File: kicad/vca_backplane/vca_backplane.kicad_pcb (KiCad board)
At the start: 4 copper layers, 147.2 x 109.9 mm, 98 parts, among them J1 Conn_02x20_Odd_Even, J10 AudioJack3DPDT, J2 Eurorack Power, J3 Conn_02x20_Odd_Even, J4 Conn_02x20_Odd_Even, J5 Conn_02x20_Odd_Even, J6 Conn_02x20_Odd_Even, J7 Conn_02x20_Odd_Even, J8 Conn_02x20_Odd_Even, J9 AudioJack3DPDT, Q1 DMMT5401, Q2 DMG2305UX, Q3 BSS138, Q4 BSS138, U1 74HCT138, U10 NE5532, U11 74HCT138, U12 MAX333A, U13 MAX333A, U14 NE5532, U2 74HCT245, U3 74LVC245, U4 MCP4822, U5 PCA9555PW, U7 AS3360, U8 M24C02-WMN, U9 PS508

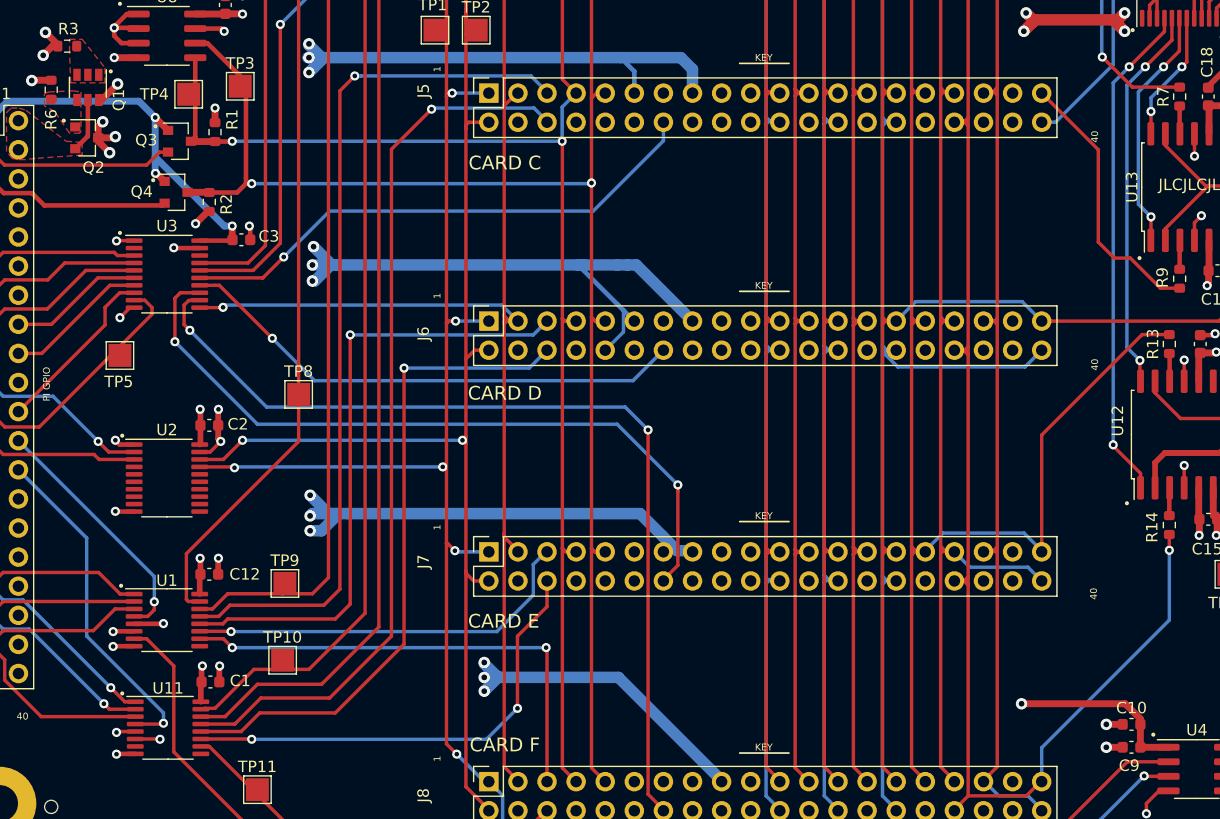
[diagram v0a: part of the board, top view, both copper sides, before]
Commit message: fix library dependency
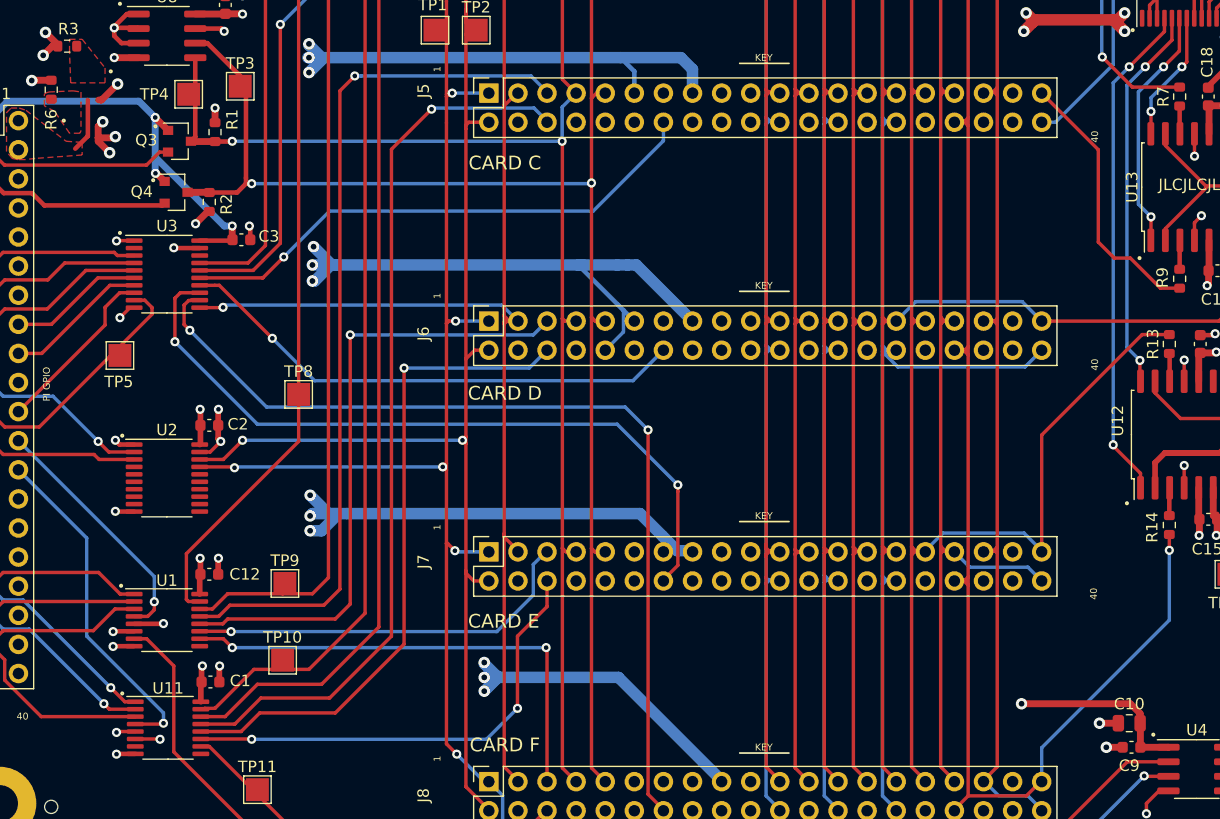
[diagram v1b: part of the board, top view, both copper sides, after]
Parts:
- removed Q1: DMMT5401, Package_TO_SOT_SMD:SOT-23-6
- removed Q2: DMG2305UX, Package_TO_SOT_SMD:SOT-23
- C10: footprint Capacitor_SMD:C_0603_1608Metric -> Capacitor_SMD:C_0805_2012Metric
- moved C10 0.22 mm to (132.9, 131.9)

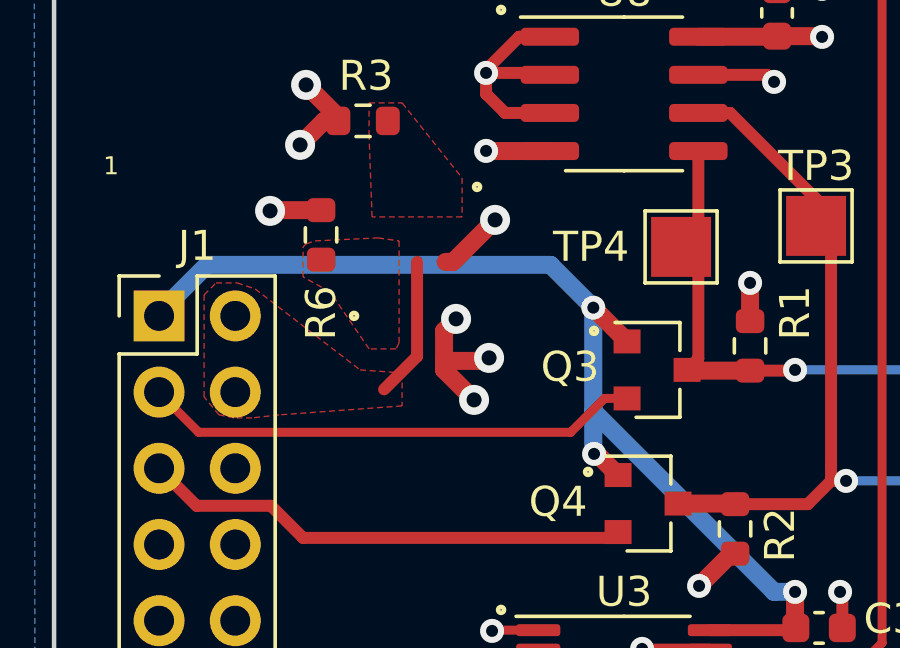
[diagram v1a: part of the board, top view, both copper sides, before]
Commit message: add missing components after library fix
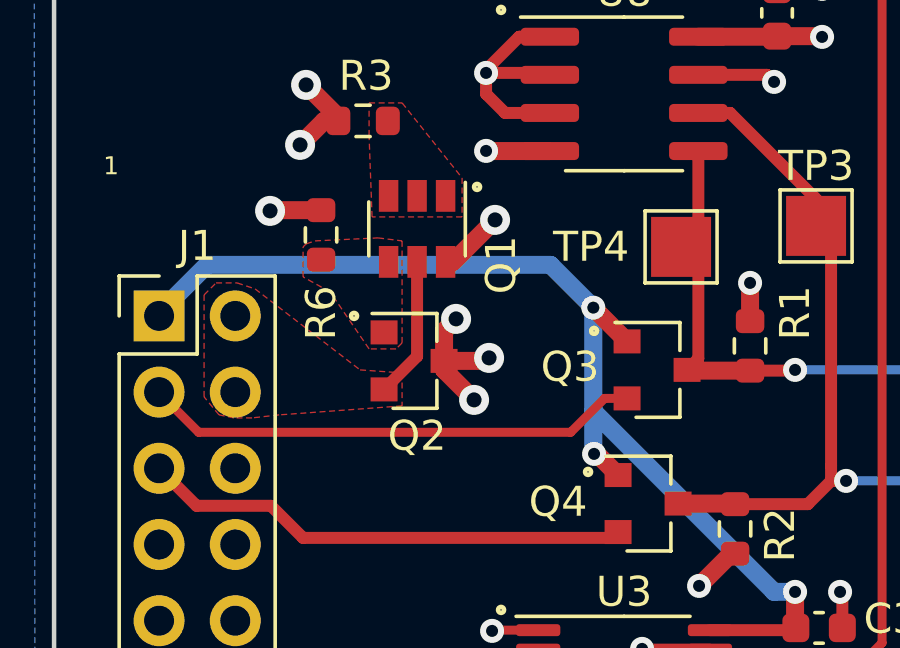
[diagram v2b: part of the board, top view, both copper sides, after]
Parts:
- added Q1: DMMT5401, Package_TO_SOT_SMD:SOT-23-6, F.Cu at (42.0, 76.4)
- added Q2: DMG2305UX, Package_TO_SOT_SMD:SOT-23, F.Cu at (41.9, 80.8)
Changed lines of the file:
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@@
     (tracks 2272)
     (zones 0)
-    (modules 96)
+    (modules 98)
     (nets 163)
   )
@@
   )
   (setup
-    (last_trace_width 0.6)
+    (last_trace_width 0.4)
     (user_trace_width 0.2)
     (user_trace_width 0.3)
@@
   (net 159 "Net-(R11-Pad2)")
   (net 160 "Net-(D1-Pad1)")
-  (net 161 "Net-(R3-Pad1)")
-  (net 162 "Net-(R6-Pad1)")
+  (net 161 "Net-(Q1-Pad4)")
+  (net 162 "Net-(Q1-Pad1)")
   (net_class Default "This is the default net class."
     (clearance 0.2)
@@
     (add_net "Net-(J9-Pad8)")
     (add_net "Net-(J9-Pad9)")
+    (add_net "Net-(Q1-Pad1)")
+    (add_net "Net-(Q1-Pad4)")
     (add_net "Net-(R10-Pad2)")
     (add_net "Net-(R11-Pad2)")
@@
     (add_net "Net-(R13-Pad1)")
     (add_net "Net-(R14-Pad1)")
-    (add_net "Net-(R3-Pad1)")
     (add_net "Net-(R4-Pad2)")
     (add_net "Net-(R5-Pad1)")
-    (add_net "Net-(R6-Pad1)")
     (add_net "Net-(R7-Pad1)")
     (add_net "Net-(R9-Pad1)")
@@
     (add_net "Net-(U9-Pad9)")
   )
+  (module Package_TO_SOT_SMD:SOT-23 (layer F.Cu)
+    (at 41.9 80.8)
+    (descr "SOT-23, Standard")
+    (tags SOT-23)
+    (attr smd)
+    (fp_text reference Q2 (at 0.1 2.5) (layer F.SilkS)
+      (effects (font (size 1 1) (thickness 0.15)))
+    )
+    (fp_text value DMG2305UX (at 0 2.5) (layer F.Fab)
+      (effects (font (size 1 1) (thickness 0.15)))
+    )
+    (fp_line (start 0.76 1.58) (end -0.7 1.58) (layer F.SilkS) (width 0.12))
+    (fp_line (start 0.76 -1.58) (end -1.4 -1.58) (layer F.SilkS) (width 0.12))
+    (fp_line (start -1.7 1.75) (end -1.7 -1.75) (layer F.CrtYd) (width 0.05))
+    (fp_line (start 1.7 1.75) (end -1.7 1.75) (layer F.CrtYd) (width 0.05))
+    (fp_line (start 1.7 -1.75) (end 1.7 1.75) (layer F.CrtYd) (width 0.05))
+    (fp_line (start -1.7 -1.75) (end 1.7 -1.75) (layer F.CrtYd) (width 0.05))
+    (fp_line (start 0.76 -1.58) (end 0.76 -0.65) (layer F.SilkS) (width 0.12))
+    (fp_line (start 0.76 1.58) (end 0.76 0.65) (layer F.SilkS) (width 0.12))
+    (fp_line (start -0.7 1.52) (end 0.7 1.52) (layer F.Fab) (width 0.1))
+    (fp_line (start 0.7 -1.52) (end 0.7 1.52) (layer F.Fab) (width 0.1))
+    (fp_line (start -0.7 -0.95) (end -0.15 -1.52) (layer F.Fab) (width 0.1))
+    (fp_line (start -0.15 -1.52) (end 0.7 -1.52) (layer F.Fab) (width 0.1))
+    (fp_line (start -0.7 -0.95) (end -0.7 1.5) (layer F.Fab) (width 0.1))
+    (fp_text user %R (at 0 0 90) (layer F.Fab)
+      (effects (font (size 0.5 0.5) (thickness 0.075)))
+    )
+    (pad 3 smd rect (at 1 0) (size 0.9 0.8) (layers F.Cu F.Paste F.Mask)
+      (net 5 +5V))
+    (pad 2 smd rect (at -1 0.95) (size 0.9 0.8) (layers F.Cu F.Paste F.Mask)
+      (net 2 /P5V_HAT))
+    (pad 1 smd rect (at -1 -0.95) (size 0.9 0.8) (layers F.Cu F.Paste F.Mask)
+      (net 161 "Net-(Q1-Pad4)"))
+    (model ${KISYS3DMOD}/Package_TO_SOT_SMD.3dshapes/SOT-23.wrl
+      (at (xyz 0 0 0))
+      (scale (xyz 1 1 1))
+      (rotate (xyz 0 0 0))
+    )
+  )
+  (module Package_TO_SOT_SMD:SOT-23-6 (layer F.Cu)
+    (at 42 76.4 270)
+    (descr "6-pin SOT-23 package")
+    (tags SOT-23-6)
+    (attr smd)
+    (fp_text reference Q1 (at 1.2 -2.8 90) (layer F.SilkS)
+      (effects (font (size 1 1) (thickness 0.15)))
+    )
+    (fp_text value DMMT5401 (at 0 2.9 90) (layer F.Fab)
+      (effects (font (size 1 1) (thickness 0.15)))
+    )
+    (fp_line (start 0.9 -1.55) (end 0.9 1.55) (layer F.Fab) (width 0.1))
+    (fp_line (start 0.9 1.55) (end -0.9 1.55) (layer F.Fab) (width 0.1))
+    (fp_line (start -0.9 -0.9) (end -0.9 1.55) (layer F.Fab) (width 0.1))
+    (fp_line (start 0.9 -1.55) (end -0.25 -1.55) (layer F.Fab) (width 0.1))
+    (fp_line (start -0.9 -0.9) (end -0.25 -1.55) (layer F.Fab) (width 0.1))
+    (fp_line (start -1.9 -1.8) (end -1.9 1.8) (layer F.CrtYd) (width 0.05))
+    (fp_line (start -1.9 1.8) (end 1.9 1.8) (layer F.CrtYd) (width 0.05))
+    (fp_line (start 1.9 1.8) (end 1.9 -1.8) (layer F.CrtYd) (width 0.05))
+    (fp_line (start 1.9 -1.8) (end -1.9 -1.8) (layer F.CrtYd) (width 0.05))
+    (fp_line (start 0.9 -1.61) (end -1.55 -1.61) (layer F.SilkS) (width 0.12))
+    (fp_line (start -0.9 1.61) (end 0.9 1.61) (layer F.SilkS) (width 0.12))
+    (fp_text user %R (at 0 0) (layer F.Fab)
+      (effects (font (size 0.5 0.5) (thickness 0.075)))
+    )
+    (pad 5 smd rect (at 1.1 0 270) (size 1.06 0.65) (layers F.Cu F.Paste F.Mask)
+      (net 2 /P5V_HAT))
+    (pad 6 smd rect (at 1.1 -0.95 270) (size 1.06 0.65) (layers F.Cu F.Paste F.Mask)
+      (net 5 +5V))
+    (pad 4 smd rect (at 1.1 0.95 270) (size 1.06 0.65) (layers F.Cu F.Paste F.Mask)
+      (net 161 "Net-(Q1-Pad4)"))
+    (pad 3 smd rect (at -1.1 0.95 270) (size 1.06 0.65) (layers F.Cu F.Paste F.Mask)
+      (net 162 "Net-(Q1-Pad1)"))
+    (pad 2 smd rect (at -1.1 0 270) (size 1.06 0.65) (layers F.Cu F.Paste F.Mask)
+      (net 162 "Net-(Q1-Pad1)"))
+    (pad 1 smd rect (at -1.1 -0.95 270) (size 1.06 0.65) (layers F.Cu F.Paste F.Mask)
+      (net 162 "Net-(Q1-Pad1)"))
+    (model ${KISYS3DMOD}/Package_TO_SOT_SMD.3dshapes/SOT-23-6.wrl
+      (at (xyz 0 0 0))
+      (scale (xyz 1 1 1))
+      (rotate (xyz 0 0 0))
+    )
+  )
   (module Capacitor_SMD:C_0805_2012Metric (layer F.Cu)
     (at 132.9 131.9)
@@
       (effects (font (size 1 1) (thickness 0.15)))
     )
-    (fp_text user %R (at 0 0) (layer F.Fab)
-      (effects (font (size 0.5 0.5) (thickness 0.08)))
-    )
     (fp_line (start -1 0.625) (end -1 -0.625) (layer F.Fab) (width 0.1))
     (fp_line (start -1 -0.625) (end 1 -0.625) (layer F.Fab) (width 0.1))
@@
     (fp_line (start 1.7 -0.98) (end 1.7 0.98) (layer F.CrtYd) (width 0.05))
     (fp_line (start 1.7 0.98) (end -1.7 0.98) (layer F.CrtYd) (width 0.05))
+    (fp_text user %R (at 0 0) (layer F.Fab)
+      (effects (font (size 0.5 0.5) (thickness 0.08)))
+    )
     (pad 2 smd roundrect (at 0.95 0) (size 1 1.45) (layers F.Cu F.Paste F.Mask) (roundrect_rratio 0.25)
       (net 5 +5V))
@@
       (net 1 GND))
     (pad 1 smd roundrect (at -0.825 0 90) (size 0.8 0.95) (layers F.Cu F.Paste F.Mask) (roundrect_rratio 0.25)
-      (net 162 "Net-(R6-Pad1)"))
+      (net 161 "Net-(Q1-Pad4)"))
     (model ${KISYS3DMOD}/Resistor_SMD.3dshapes/R_0603_1608Metric.wrl
       (at (xyz 0 0 0))
@@
       (net 1 GND))
     (pad 1 smd roundrect (at -0.825 0 180) (size 0.8 0.95) (layers F.Cu F.Paste F.Mask) (roundrect_rratio 0.25)
-      (net 161 "Net-(R3-Pad1)"))
+      (net 162 "Net-(Q1-Pad1)"))
     (model ${KISYS3DMOD}/Resistor_SMD.3dshapes/R_0603_1608Metric.wrl
       (at (xyz 0 0 0))
@@
     )
   )
-  (zone (net 161) (net_name "Net-(R3-Pad1)") (layer F.Cu) (hatch edge 0.508)
+  (zone (net 162) (net_name "Net-(Q1-Pad1)") (layer F.Cu) (hatch edge 0.508)
     (connect_pads yes (clearance 0.4))
     (min_thickness 0.254)
@@
     )
   )
-  (zone (net 162) (net_name "Net-(R6-Pad1)") (layer F.Cu) (hatch edge 0.508)
+  (zone (net 161) (net_name "Net-(Q1-Pad4)") (layer F.Cu) (hatch edge 0.508)
     (connect_pads yes (clearance 0.4))
     (min_thickness 0.254)
@@
       (pts
         (xy 41.3 80.4) (xy 40.4 80.4) (xy 39.1 78.5) (xy 38.2 78) (xy 38.2 77)
-        (xy 38.3 76.9) (xy 38.6 76.8) (xy 40.7 76.7) (xy 41.4 76.8) (xy 41.4 80.2)
+        (xy 38.3 76.9) (xy 38.6 76.8) (xy 40.7 76.7) (xy 41.5 76.8) (xy 41.5 80.2)
       )
     )

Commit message: kicad6 commit
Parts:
- added C27: 47u, Capacitor_THT:CP_Radial_D6.3mm_P2.50mm, F.Cu at (182.8, 114.0)
- added C28: 47u, Capacitor_THT:CP_Radial_D6.3mm_P2.50mm, F.Cu at (190.8, 114.0)
- added R23: 2k, Resistor_SMD:R_0603_1608Metric, F.Cu at (182.0, 119.2)
- added R25: 2k, Resistor_SMD:R_0603_1608Metric, F.Cu at (186.0, 119.2)
- moved R11 26.2 mm to (136.4, 35.7), turned to 0 degrees
- moved D1 25.4 mm to (132.9, 35.7)
- moved C22 12.6 mm to (158.9, 114.8), turned to 180 degrees
- moved C24 12.4 mm to (157.7, 99.0), turned to 180 degrees
- moved C25 11.6 mm to (168.7, 94.4)
- moved C23 10.9 mm to (169.9, 108.8), turned to 90 degrees
- moved G*** 2.50 mm to (154.2, 37.5), turned to 180 degrees
- moved J10 1.95 mm to (162.8, 53.6)
- moved J9 1.95 mm to (162.8, 77.1)
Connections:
- C26 pad 1: Net-(C26-Pad1) -> GND
- C26 pad 2: GND -> Net-(C26-Pad2)
- C4 pad 1: GND -> Net-(C4-Pad1)
- C4 pad 2: Net-(C4-Pad2) -> GND
- J1 pad 10: Net-(J1-Pad10) -> unconnected-(J1-Pad10)
- J1 pad 12: Net-(J1-Pad12) -> unconnected-(J1-Pad12)
- J1 pad 17: Net-(J1-Pad17) -> unconnected-(J1-Pad17)
- J1 pad 29: Net-(J1-Pad29) -> unconnected-(J1-Pad29)
- J1 pad 31: Net-(J1-Pad31) -> unconnected-(J1-Pad31)
- J1 pad 32: Net-(J1-Pad32) -> unconnected-(J1-Pad32)
- J1 pad 36: Net-(J1-Pad36) -> unconnected-(J1-Pad36)
- J1 pad 38: Net-(J1-Pad38) -> unconnected-(J1-Pad38)
- J1 pad 40: Net-(J1-Pad40) -> unconnected-(J1-Pad40)
- J1 pad 7: Net-(J1-Pad7) -> unconnected-(J1-Pad7)
- J1 pad 8: Net-(J1-Pad8) -> unconnected-(J1-Pad8)
- J10 pad 3: Net-(J10-Pad3) -> unconnected-(J10-Pad3)
- J10 pad 4: Net-(J10-Pad4) -> unconnected-(J10-Pad4)
- J10 pad 5: Net-(J10-Pad5) -> unconnected-(J10-Pad5)
- J10 pad 6: Net-(J10-Pad6) -> unconnected-(J10-Pad6)
- J10 pad 9: Net-(J10-Pad9) -> unconnected-(J10-Pad9)
- J2 pad 13: Net-(J2-Pad13) -> unconnected-(J2-Pad13)
- J2 pad 14: Net-(J2-Pad14) -> unconnected-(J2-Pad14)
- J2 pad 15: Net-(J2-Pad15) -> unconnected-(J2-Pad15)
- J2 pad 16: Net-(J2-Pad16) -> unconnected-(J2-Pad16)
- J3 pad 37: Net-(J3-Pad37) -> unconnected-(J3-Pad37)
- J4 pad 37: Net-(J4-Pad37) -> unconnected-(J4-Pad37)
- J5 pad 37: Net-(J5-Pad37) -> unconnected-(J5-Pad37)
- J6 pad 37: Net-(J6-Pad37) -> unconnected-(J6-Pad37)
- J7 pad 37: Net-(J7-Pad37) -> unconnected-(J7-Pad37)
- J8 pad 37: Net-(J8-Pad37) -> unconnected-(J8-Pad37)
- J9 pad 7: Net-(J9-Pad7) -> unconnected-(J9-Pad7)
- J9 pad 8: Net-(J9-Pad8) -> unconnected-(J9-Pad8)
- J9 pad 9: Net-(J9-Pad9) -> unconnected-(J9-Pad9)
- R10 pad 1: Net-(C26-Pad1) -> Net-(C26-Pad2)
- R4 pad 1: Net-(C4-Pad2) -> Net-(C4-Pad1)
- RV1 pad 1: Net-(C26-Pad1) -> GND
- RV1 pad 3: GND -> Net-(C26-Pad2)
- RV1 pad 4: Net-(C4-Pad2) -> GND
- RV1 pad 6: GND -> Net-(C4-Pad1)
- TP13 pad 1: Net-(C4-Pad2) -> Net-(C4-Pad1)
- TP14 pad 1: Net-(C26-Pad1) -> Net-(C26-Pad2)
- U1 pad 9: Net-(U1-Pad9) -> unconnected-(U1-Pad9)
- U10 pad 4: +12V -> -12V
- U10 pad 8: -12V -> +12V
- U11 pad 9: Net-(U11-Pad9) -> unconnected-(U11-Pad9)
- U12 pad 15: Net-(U12-Pad15) -> unconnected-(U12-Pad15)
- U13 pad 15: Net-(U13-Pad15) -> unconnected-(U13-Pad15)
- U14 pad 4: +12V -> -12V
- U14 pad 8: -12V -> +12V
- U2 pad 11: Net-(U2-Pad11) -> unconnected-(U2-Pad11)
- U2 pad 12: Net-(U2-Pad12) -> unconnected-(U2-Pad12)
- U2 pad 13: Net-(U2-Pad13) -> unconnected-(U2-Pad13)
- U2 pad 14: Net-(U2-Pad14) -> unconnected-(U2-Pad14)
- U2 pad 15: Net-(U2-Pad15) -> unconnected-(U2-Pad15)
- U2 pad 16: Net-(U2-Pad16) -> unconnected-(U2-Pad16)
- U2 pad 4: Net-(U2-Pad4) -> unconnected-(U2-Pad4)
- U2 pad 5: Net-(U2-Pad5) -> unconnected-(U2-Pad5)
- U2 pad 6: Net-(U2-Pad6) -> unconnected-(U2-Pad6)
- U2 pad 7: Net-(U2-Pad7) -> unconnected-(U2-Pad7)
- U2 pad 8: Net-(U2-Pad8) -> unconnected-(U2-Pad8)
- U2 pad 9: Net-(U2-Pad9) -> unconnected-(U2-Pad9)
- U3 pad 18: Net-(U3-Pad18) -> unconnected-(U3-Pad18)
- U3 pad 2: Net-(U3-Pad2) -> unconnected-(U3-Pad2)
- U5 pad 1: Net-(U5-Pad1) -> unconnected-(U5-Pad1)
- U5 pad 16: Net-(U5-Pad16) -> unconnected-(U5-Pad16)
- U5 pad 17: Net-(U5-Pad17) -> unconnected-(U5-Pad17)
- U5 pad 18: Net-(U5-Pad18) -> unconnected-(U5-Pad18)
- U7 pad 6: Net-(U12-Pad8) -> Net-(U7-Pad6)
- U7 pad 9: Net-(U12-Pad13) -> Net-(U7-Pad9)
- U9 pad 10: Net-(U9-Pad10) -> unconnected-(U9-Pad10)
- U9 pad 9: Net-(U9-Pad9) -> unconnected-(U9-Pad9)
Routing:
- net +12V: track 432.1 -> 340.2 mm, vias 13 -> 10
- net -12V: track 431.5 -> 381.4 mm, vias 6 -> 5
- net Net-(C26-Pad1): track 29.2 -> 0.00 mm
- net Net-(R11-Pad2): track 2.31 -> 31.3 mm, vias 0 -> 2
- net Net-(U7-Pad9): track 0.00 -> 25.6 mm, vias 0 -> 2
- net Net-(U12-Pad13): track 25.6 -> 0.00 mm, vias 2 -> 0
- net Net-(J10-Pad8): track 25.1 -> 0.00 mm
- net /Sheet624DD88D/RIGHT: track 38.7 -> 14.3 mm
- net Net-(C4-Pad2): track 22.6 -> 0.00 mm
- net Net-(J10-Pad2): track 21.6 -> 0.00 mm
- net /Sheet624DD88D/MONO: track 36.5 -> 19.3 mm
- net Net-(C26-Pad2): track 0.00 -> 13.4 mm, vias 0 -> 1
- net GND: track 1073.0 -> 1060.5 mm, vias 52 -> 46
- net Net-(U7-Pad6): track 0.00 -> 11.3 mm
- net Net-(U12-Pad8): track 11.3 -> 0.00 mm
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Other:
- net class Default removed
